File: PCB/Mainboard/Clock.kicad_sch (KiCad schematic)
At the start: 34 parts, among them Q31 6D, U16 QC01, U62 74LS125, U63 AV9154A-27, U66 SN74LV02, X4 59G3482

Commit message: Add files via upload
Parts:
- removed unit 2 of U66
- removed unit 1 of U66
- removed unit 3 of U66
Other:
- moved on the sheet: C227, C230, C232, C257, C258, C259, C260, C261, C56, C59, D9, Q31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

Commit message: Add files via upload
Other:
- company: (none) -> Recreated by: Ahmad Byagowi
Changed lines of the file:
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@@
 	(title_block
 		(title "PC110")
+		(company "Recreated by: Ahmad Byagowi")
 	)
 	(junction

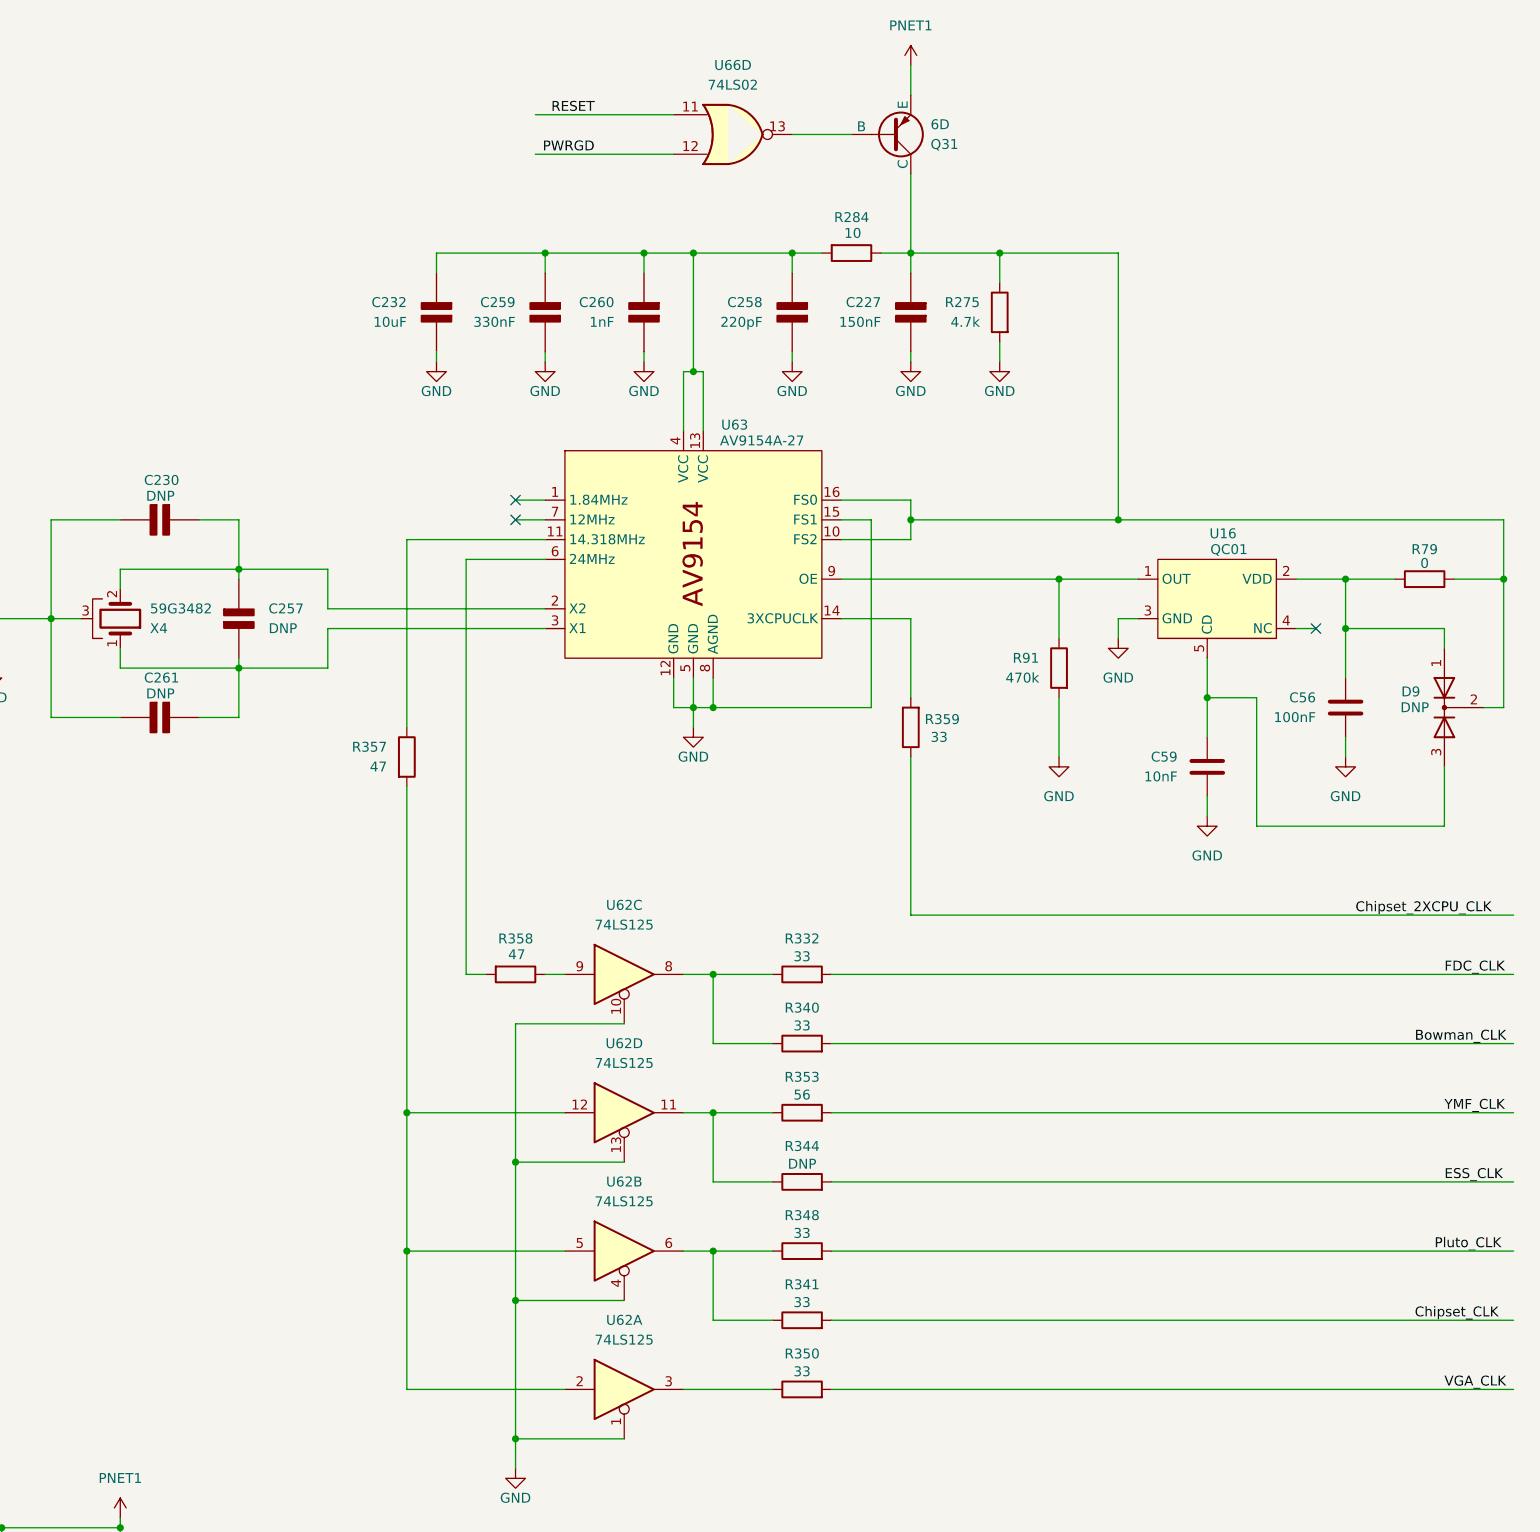
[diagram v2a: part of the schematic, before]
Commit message: Add part numbers to some SMT parts
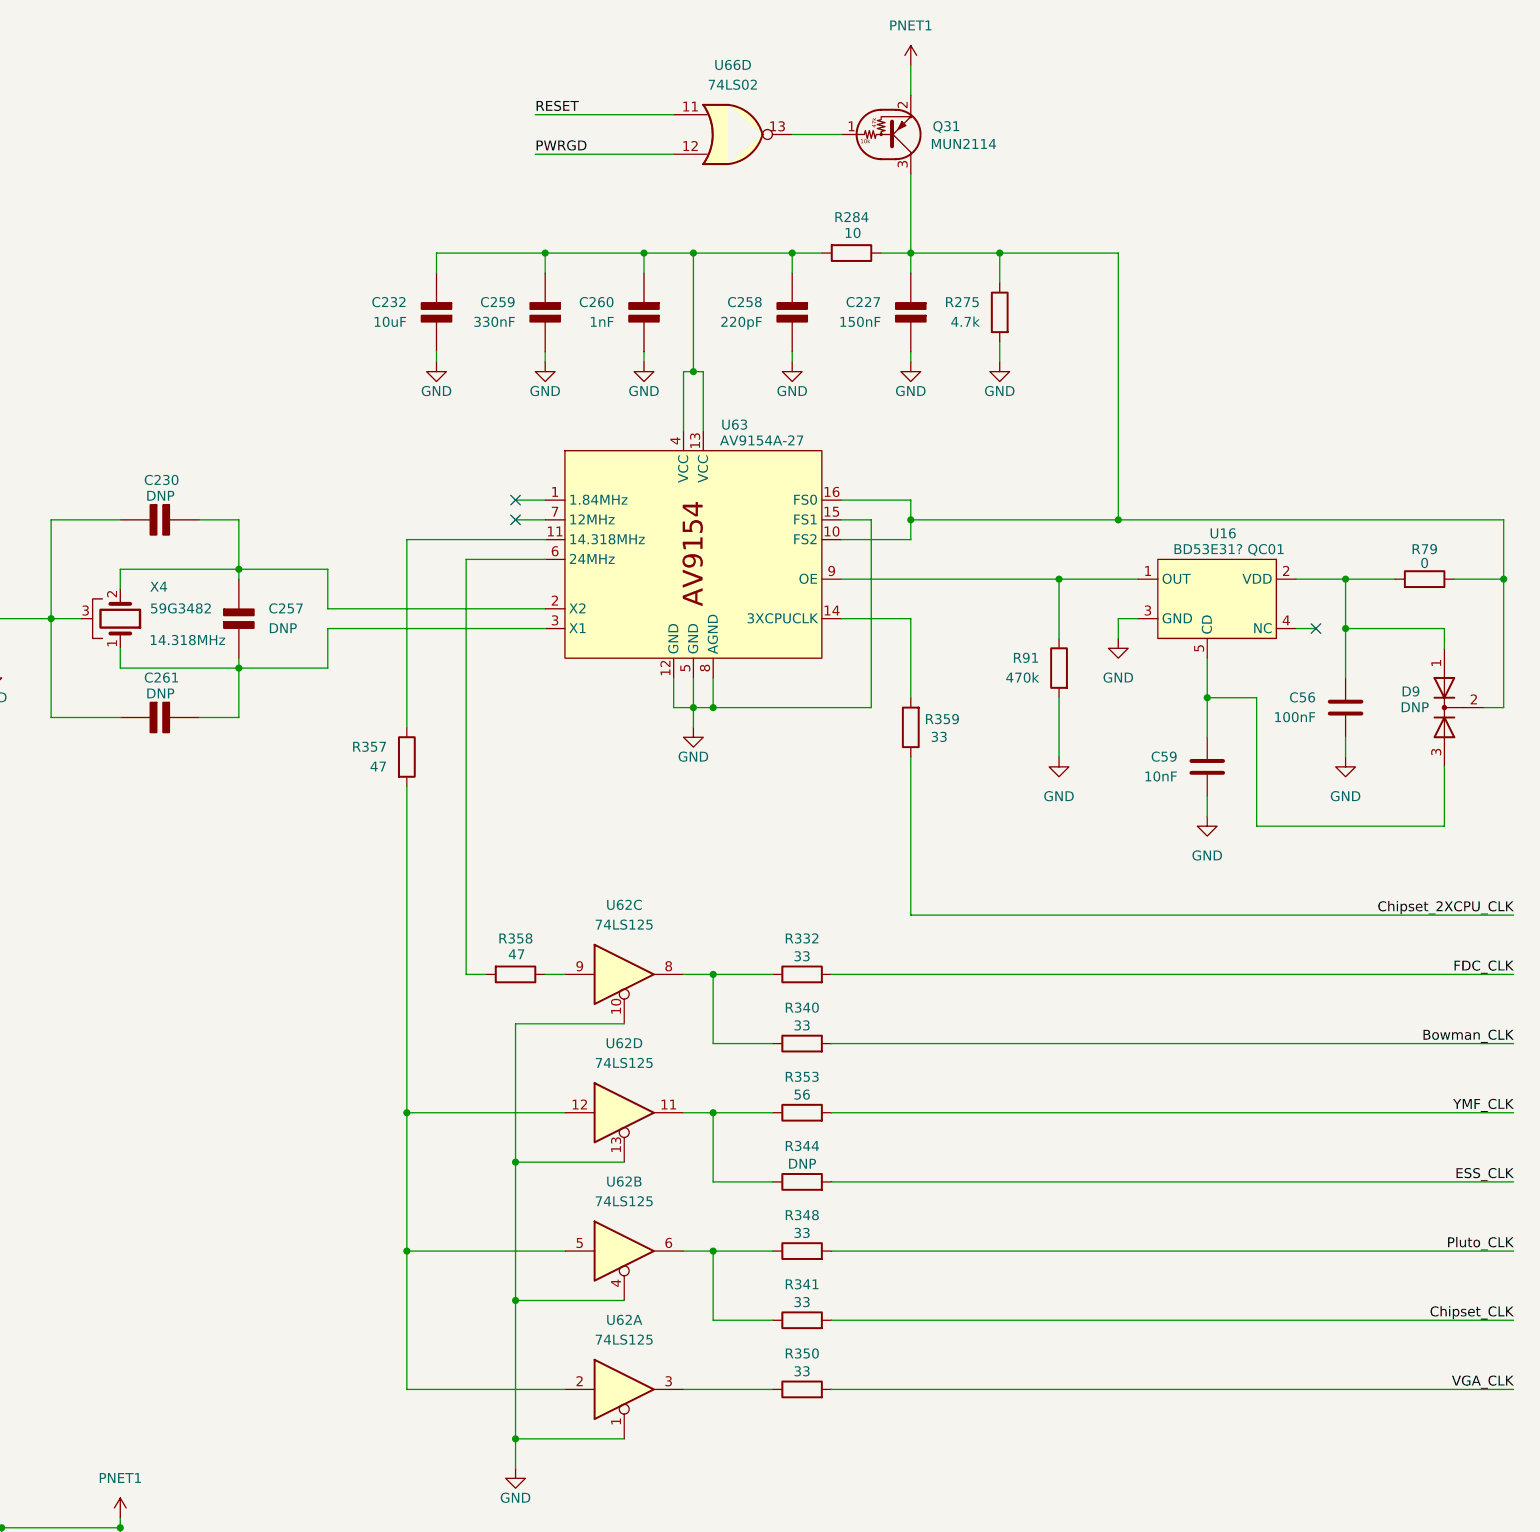
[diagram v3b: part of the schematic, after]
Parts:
- removed Q31: 6D, symbol Simulation_SPICE:PNP
- added Q31: MUN2114, symbol Transistor_BJT:DTA114Y
- U16: value QC01 -> BD53E31? QC01
- X4: Frequency (none) -> 14.318MHz
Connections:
- net PNET1: now also Q31.2 (E)
- net at C227.1 (+), D9.2 (K), R275.1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: now also Q31.3 (C)
- net at U66.13: now also Q31.1 (B)
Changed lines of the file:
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@@
 	(wire
 		(pts
+			(xy 194.31 50.8) (xy 187.96 50.8)
+		)
+		(stroke
+			(width 0)
+			(type default)
+		)
+	)
+	(wire
+		(pts
 			(xy 52.07 256.54) (xy 52.07 257.81)
 		)
@@
 	(wire
 		(pts
-			(xy 195.58 50.8) (xy 187.96 50.8)
-		)
-		(stroke
-			(width 0)
-			(type default)
-		)
-	)
-	(wire
-		(pts
 			(xy 198.12 124.46) (xy 177.8 124.46)
 		)
@@
 	)
 	(label "Bowman_CLK"
-		(at 267.97 167.64 0)
+		(at 280.67 167.64 180)
 		(effects
 			(font
 				(size 1.27 1.27)
 			)
-			(justify left bottom)
+			(justify right bottom)
 		)
 	)
 	(label "ESS_CLK"
-		(at 271.78 185.42 0)
+		(at 280.67 185.42 180)
 		(effects
 			(font
 				(size 1.27 1.27)
 			)
-			(justify left bottom)
+			(justify right bottom)
 		)
 	)
 	(label "FDC_CLK"
-		(at 271.78 158.75 0)
+		(at 280.67 158.75 180)
 		(effects
 			(font
 				(size 1.27 1.27)
 			)
-			(justify left bottom)
+			(justify right bottom)
 		)
 	)
 	(label "PWRGD"
-		(at 162.56 53.34 180)
+		(at 154.94 53.34 0)
 		(effects
 			(font
 				(size 1.27 1.27)
 			)
-			(justify right bottom)
+			(justify left bottom)
 		)
 	)
 	(label "VGA_CLK"
-		(at 271.78 212.09 0)
+		(at 280.67 212.09 180)
 		(effects
 			(font
 				(size 1.27 1.27)
 			)
-			(justify left bottom)
+			(justify right bottom)
 		)
 	)
 	(label "RESET"
-		(at 162.56 48.26 180)
+		(at 154.94 48.26 0)
 		(effects
 			(font
 				(size 1.27 1.27)
 			)
-			(justify right bottom)
+			(justify left bottom)
 		)
 	)
 	(label "Chipset_CLK"
-		(at 267.97 203.2 0)
+		(at 280.67 203.2 180)
 		(effects
 			(font
 				(size 1.27 1.27)
 			)
-			(justify left bottom)
+			(justify right bottom)
 		)
 	)
 	(label "YMF_CLK"
-		(at 271.78 176.53 0)
+		(at 280.67 176.53 180)
 		(effects
 			(font
 				(size 1.27 1.27)
 			)
-			(justify left bottom)
+			(justify right bottom)
 		)
 	)
 	(label "Pluto_CLK"
-		(at 270.51 194.31 0)
+		(at 280.67 194.31 180)
 		(effects
 			(font
 				(size 1.27 1.27)
 			)
-			(justify left bottom)
+			(justify right bottom)
 		)
 	)
 	(label "Chipset_2XCPU_CLK"
-		(at 260.35 151.13 0)
+		(at 280.67 151.13 180)
 		(effects
 			(font
 				(size 1.27 1.27)
 			)
-			(justify left bottom)
+			(justify right bottom)
 		)
 	)
@@
 	)
 	(symbol
+		(lib_id "Transistor_BJT:DTA114Y")
+		(at 200.66 50.8 0)
+		(mirror x)
+		(unit 1)
+		(exclude_from_sim no)
+		(in_bom yes)
+		(on_board yes)
+		(dnp no)
+		(property "Reference" "Q31"
+			(at 205.994 49.7839 0)
+			(effects
+				(font
+					(size 1.27 1.27)
+				)
+				(justify left)
+			)
+		)
+		(property "Value" "MUN2114"
+			(at 205.74 52.07 0)
+			(effects
+				(font
+					(size 1.27 1.27)
+				)
+				(justify left)
+			)
+		)
+		(property "Footprint" ""
+			(at 200.66 50.8 0)
+			(effects
+				(font
+					(size 1.27 1.27)
+				)
+				(justify left)
+				(hide yes)
+			)
+		)
+		(property "Datasheet" ""
+			(at 200.66 50.8 0)
+			(effects
+				(font
+					(size 1.27 1.27)
+				)
+				(justify left)
+				(hide yes)
+			)
+		)
+		(property "Description" "Digital PNP Transistor, 10k/47k, SOT-23"
+			(at 200.66 50.8 0)
+			(effects
+				(font
+					(size 1.27 1.27)
+				)
+				(hide yes)
+			)
+		)
+		(property "Topmark" "6D"
+			(at 200.66 50.8 0)
+			(effects
+				(font
+					(size 1.27 1.27)
+				)
+				(hide yes)
+			)
+		)
+		(pin "2"
+		)
+		(pin "3"
+		)
+		(pin "1"
+		)
+		(instances
+			(project ""
+				(path "/45c7911f-b027-440e-9e3e-77a146b41944/8c702c69-d3f6-4026-9af8-e972f7ced597"
+					(reference "Q31")
+					(unit 1)
+				)
+			)
+		)
+	)
+	(symbol
 		(lib_id "PCM_Elektuur:C")
 		(at 168.91 73.66 0)
@@
 			)
 		)
-		(property "Value" "QC01"
+		(property "Value" "BD53E31? QC01"
 			(at 244.094 104.14 0)
 			(effects
@@
 		(dnp no)
 		(property "Reference" "X4"
-			(at 105.41 114.3001 90)
+			(at 105.41 108.966 90)
 			(effects
 				(font
@@
 			)
 		)
+		(property "Frequency" "14.318MHz"
+			(at 110.236 115.824 90)
+			(effects
+				(font
+					(size 1.27 1.27)
+				)
+			)
+		)
 		(pin "1"
 		)
@@
 					(unit 1)
 				)
-			)
-		)
-	)
-	(symbol
-		(lib_id "Simulation_SPICE:PNP")
-		(at 200.66 50.8 0)
-		(mirror x)
-		(unit 1)
-		(exclude_from_sim no)
-		(in_bom yes)
-		(on_board yes)
-		(dnp no)
-		(property "Reference" "Q31"
-			(at 205.74 52.0701 0)
-			(effects
-				(font
-					(size 1.27 1.27)
-				)
-				(justify left)
-			)
-		)
-		(property "Value" "6D"
-			(at 205.74 49.5301 0)
-			(effects
-				(font
-					(size 1.27 1.27)
-				)
-				(justify left)
-			)
-		)
-		(property "Footprint" ""
-			(at 236.22 50.8 0)
-			(effects
-				(font
-					(size 1.27 1.27)
-				)
-				(hide yes)
-			)
-		)
-		(property "Datasheet" "https://ngspice.sourceforge.io/docs/ngspice-html-manual/manual.xhtml#cha_BJTs"
-			(at 236.22 50.8 0)
-			(effects
-				(font
-					(size 1.27 1.27)
-				)
-				(hide yes)
-			)
-		)
-		(property "Description" "Bipolar transistor symbol for simulation only, substrate tied to the emitter"
-			(at 200.66 50.8 0)
-			(effects
-				(font
-					(size 1.27 1.27)
-				)
-				(hide yes)
-			)
-		)
-		(property "Sim.Device" "PNP"
-			(at 200.66 50.8 0)
-			(effects
-				(font
-					(size 1.27 1.27)
-				)
-				(hide yes)
-			)
-		)
-		(property "Sim.Type" "GUMMELPOON"
-			(at 200.66 50.8 0)
-			(effects
-				(font
-					(size 1.27 1.27)
-				)
-				(hide yes)
-			)
-		)
-		(property "Sim.Pins" "1=C 2=B 3=E"
-			(at 200.66 50.8 0)
-			(effects
-				(font
-					(size 1.27 1.27)
-				)
-				(hide yes)
-			)
-		)
-		(pin "1"
-		)
-		(pin "3"
-		)
-		(pin "2"
-		)
-		(instances
-			(project "PC110"
-				(path "/45c7911f-b027-440e-9e3e-77a146b41944/8c702c69-d3f6-4026-9af8-e972f7ced597"
-					(reference "Q31")
-					(unit 1)
-				)
